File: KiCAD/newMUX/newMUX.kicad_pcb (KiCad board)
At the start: 4 copper layers, 17.8 x 30 mm, 13 parts, among them P1 CONN_02X07, P2 CONN_02X07, U1 MAX14662, U2 MAX14662, U3 PCF8574

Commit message: new mux done
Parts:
- removed G***: value, myParts:logo_small
- removed P1: CONN_02X07, myParts:SSM-107-L-DV
- removed P2: CONN_02X07, myParts:SSM-107-L-DV-INV
- removed R3, R4, R5, R6, R7: R, Resistors_SMD:R_0402
- added C1: 0.1uF, Capacitors_SMD:C_0603_HandSoldering, B.Cu at (47.0, -82.5)
- added J1: Conn_01x14, Pin_Headers:Pin_Header_Straight_1x14_Pitch2.54mm, B.Cu at (23.5, -61.0)
- added J2: Conn_02x06_Odd_Even, Socket_Strips:Socket_Strip_Straight_2x06_Pitch2.54mm, F.Cu at (35.9, -38.1)
- added J3: Conn_02x06_Odd_Even, Socket_Strips:Socket_Strip_Straight_2x06_Pitch2.54mm, F.Cu at (46.0, -38.1)
- added J4: Conn_01x14, Pin_Headers:Pin_Header_Straight_1x14_Pitch2.54mm, B.Cu at (61.0, -61.0)
- added JP1: Jumper_NC_Small, Connect:GS2, B.Cu at (27.9, -48.3)
- added JP2: Jumper_NC_Dual, Connect:GS3, B.Cu at (59.7, -85.1)
- added JP3: Jumper_NC_Dual, Connect:GS3, B.Cu at (57.1, -82.5)
- added JP4: Jumper_NC_Dual, Connect:GS3, B.Cu at (53.3, -85.1)
- added JP5: Jumper_NC_Dual, Connect:GS3, B.Cu at (52.1, -82.5)
- added JP6: Jumper_NC_Small, Connect:GS2, B.Cu at (57.1, -48.3)
- added L1: GREY@CHRISTOFORO.NET, myParts:logo, F.Cu at (27.3, -44.5)
- added U10: ASSR-1611, Housings_DIP:DIP-6_W7.62mm, F.Cu at (47.0, -24.1)
- added U11: ASSR-1611, Housings_DIP:DIP-6_W7.62mm, F.Cu at (31.8, -24.1)
- added U12: ASSR-1611, Housings_DIP:DIP-6_W7.62mm, F.Cu at (24.1, -68.6)
- added U13: ASSR-1611, Housings_DIP:DIP-6_W7.62mm, F.Cu at (31.8, -68.6)
- added U14: ASSR-1611, Housings_DIP:DIP-6_W7.62mm, F.Cu at (39.4, -68.6)
- added U15: ASSR-1611, Housings_DIP:DIP-6_W7.62mm, F.Cu at (47.0, -68.6)
- added U16: ASSR-1611, Housings_DIP:DIP-6_W7.62mm, F.Cu at (54.6, -68.6)
- added U17: ASSR-1611, Housings_DIP:DIP-6_W7.62mm, F.Cu at (31.8, -57.1)
- added U18: ASSR-1611, Housings_DIP:DIP-6_W7.62mm, F.Cu at (39.4, -57.1)
- added U19: ASSR-1611, Housings_DIP:DIP-6_W7.62mm, F.Cu at (47.0, -57.1)
- added U20: ASSR-1611, Housings_DIP:DIP-6_W7.62mm, F.Cu at (54.6, -12.7)
- added U21: ASSR-1611, Housings_DIP:DIP-6_W7.62mm, F.Cu at (24.1, -12.7)
- added U22: MCP23S17, Housings_DIP:DIP-28_W7.62mm, F.Cu at (25.4, -80.0)
- added U4: ASSR-1611, Housings_DIP:DIP-6_W7.62mm, F.Cu at (39.4, -1.27)
- added U5: ASSR-1611, Housings_DIP:DIP-6_W7.62mm, F.Cu at (47.0, -1.27)
- added U6: ASSR-1611, Housings_DIP:DIP-6_W7.62mm, F.Cu at (54.6, -1.27)
- added U7: ASSR-1611, Housings_DIP:DIP-6_W7.62mm, F.Cu at (31.8, -12.7)
- added U8: ASSR-1611, Housings_DIP:DIP-6_W7.62mm, F.Cu at (39.4, -12.7)
- added U9: ASSR-1611, Housings_DIP:DIP-6_W7.62mm, F.Cu at (47.0, -12.7)
- R1: value R -> 830K; footprint Resistors_SMD:R_0402 -> Resistors_SMD:R_2010_HandSoldering; moved to F.Cu
- R2: value R -> 500K; footprint Resistors_SMD:R_0402 -> Resistors_SMD:R_0805_HandSoldering
- U1, U2: value MAX14662 -> ASSR-1611; footprint Housings_DFN_QFN:QFN-28-1EP_4x4mm_Pitch0.4mm -> Housings_DIP:DIP-6_W7.62mm; moved to F.Cu
- U3: value PCF8574 -> ASSR-1611; footprint SMD_Packages:SO-16-W -> Housings_DIP:DIP-6_W7.62mm; moved to F.Cu
- moved R1 55.9 mm to (55.9, -28.6), turned to 90 degrees
- moved U1 47.8 mm to (39.4, -24.1), turned to 90 degrees
- moved R2 30.2 mm to (26.7, -24.2), turned to 90 degrees
- moved U3 21.2 mm to (31.8, -1.27), turned to 90 degrees
- moved U2 18.2 mm to (24.1, -1.27), turned to 90 degrees
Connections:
- R1 pad 1: +5V -> GND
- R1 pad 2: A0 -> /PRE_GND
- R2 pad 1: A0 -> Net-(R2-Pad1)
- R2 pad 2: GND -> V_D
- U1 pad 1: +5V -> /TOP
- U1 pad 2: L_I -> /PRE_GND
- U1 pad 3: 0_I -> (no net)
- U1 pad 4: 1_I -> V-
- U1 pad 5: 2_I -> (no net)
- U1 pad 6: 3_I -> /VT
- U2 pad 1: +5V -> /P1
- U2 pad 2: L_V -> /PRE_GND
- U2 pad 3: 0_V -> (no net)
- U2 pad 4: 1_V -> V+
- U2 pad 5: 2_V -> (no net)
- U2 pad 6: 3_V -> /V1
- U3 pad 1: A0 -> /P2
- U3 pad 2: A1 -> /PRE_GND
- U3 pad 3: A2 -> (no net)
- U3 pad 4: SM_CS -> V+
- U3 pad 5: Net-(U3-Pad5) -> (no net)
- U3 pad 6: Net-(U3-Pad6) -> /V2
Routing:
- net /PRE_GND: track 0.00 -> 196.8 mm, vias 0 -> 1
- net /BOT: track 0.00 -> 108.7 mm
- net /P3: track 0.00 -> 106.2 mm
- net /P5: track 0.00 -> 103.0 mm
- net /P4: track 0.00 -> 101.8 mm, vias 0 -> 3
- net V+: track 10.6 -> 105.6 mm
- net /P8: track 0.00 -> 87.8 mm, vias 0 -> 2
- net /TOP: track 0.00 -> 84.0 mm, vias 0 -> 3
- net /P2: track 0.00 -> 83.8 mm, vias 0 -> 1
- net /V_D_EN: track 0.00 -> 83.2 mm
- net /P7: track 0.00 -> 82.9 mm, vias 0 -> 1
- net /P1: track 0.00 -> 81.9 mm
- net V_D: track 0.00 -> 77.9 mm, vias 0 -> 2
- net /P6: track 0.00 -> 72.9 mm, vias 0 -> 2
- net MISO: track 0.00 -> 72.8 mm, vias 0 -> 2
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- added copper zone on B.Cu, net /PRE_GND
- added copper zone on F.Cu, net I+
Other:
- board size 17.8 x 30 mm -> 40 x 88.9 mm
- net class Default: clearance 0.153 -> 0.16; trace_width 0.25 -> 0.4; via_dia 0.8 -> 0.6
- rule trace_clearance: 0.153 -> 0.16
- rule trace_min: 0.18 -> 0.16
- board text removed: "17e0726"
- board text removed: "A0"
- board text removed: "A1"
- board text removed: "A2"
- board text removed: "H"
- board text removed: "L"

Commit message: generate order zip and silk for newMUX
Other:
- board text added: "ac10c1a"
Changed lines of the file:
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@@
-(kicad_pcb (version 4) (host pcbnew 4.0.6)
+(kicad_pcb (version 4) (host pcbnew 4.0.7)
   (general
     (links 127)
@@
     (area 22.149999 -88.975001 62.305001 0.075001)
     (thickness 1.6)
-    (drawings 8)
+    (drawings 9)
     (tracks 679)
     (zones 0)
@@
     (descr "6-lead dip package, row spacing 7.62 mm (300 mils)")
     (tags "DIL DIP PDIP 2.54mm 7.62mm 300mil")
-    (fp_text reference U17 (at 3.81 -2.39 90) (layer F.SilkS)
+    (fp_text reference U17 (at 3.81 0.635 90) (layer F.SilkS)
       (effects (font (size 1 1) (thickness 0.15)))
     )
@@
     (descr "6-lead dip package, row spacing 7.62 mm (300 mils)")
     (tags "DIL DIP PDIP 2.54mm 7.62mm 300mil")
-    (fp_text reference U18 (at 3.81 -2.39 90) (layer F.SilkS)
+    (fp_text reference U18 (at 3.81 0.635 90) (layer F.SilkS)
       (effects (font (size 1 1) (thickness 0.15)))
     )
@@
     (descr "6-lead dip package, row spacing 7.62 mm (300 mils)")
     (tags "DIL DIP PDIP 2.54mm 7.62mm 300mil")
-    (fp_text reference U19 (at 3.81 -2.39 90) (layer F.SilkS)
+    (fp_text reference U19 (at 3.81 0.635 90) (layer F.SilkS)
       (effects (font (size 1 1) (thickness 0.15)))
     )
@@
       (xy 8.293997 0.976563) (xy 8.491005 0.779554)) (layer F.SilkS) (width 0.001))
   )
+  (gr_text ac10c1a (at 30.48 -44.45 90) (layer F.SilkS)
+    (effects (font (size 1.5 1.5) (thickness 0.3)))
+  )
   (gr_arc (start 59.69 -2.54) (end 62.23 -2.54) (angle 90) (layer Edge.Cuts) (width 0.15))

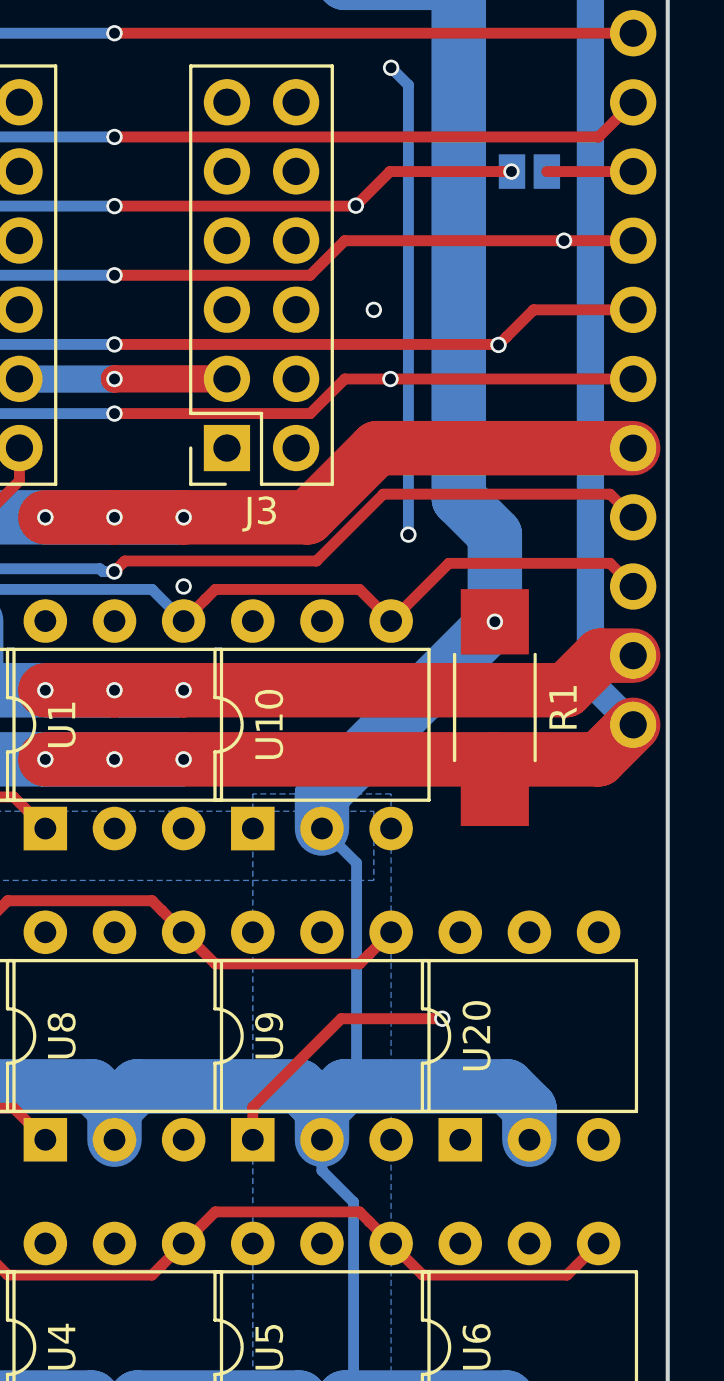
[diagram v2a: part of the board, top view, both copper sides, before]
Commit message: fixed some no-connect bugs in newMux
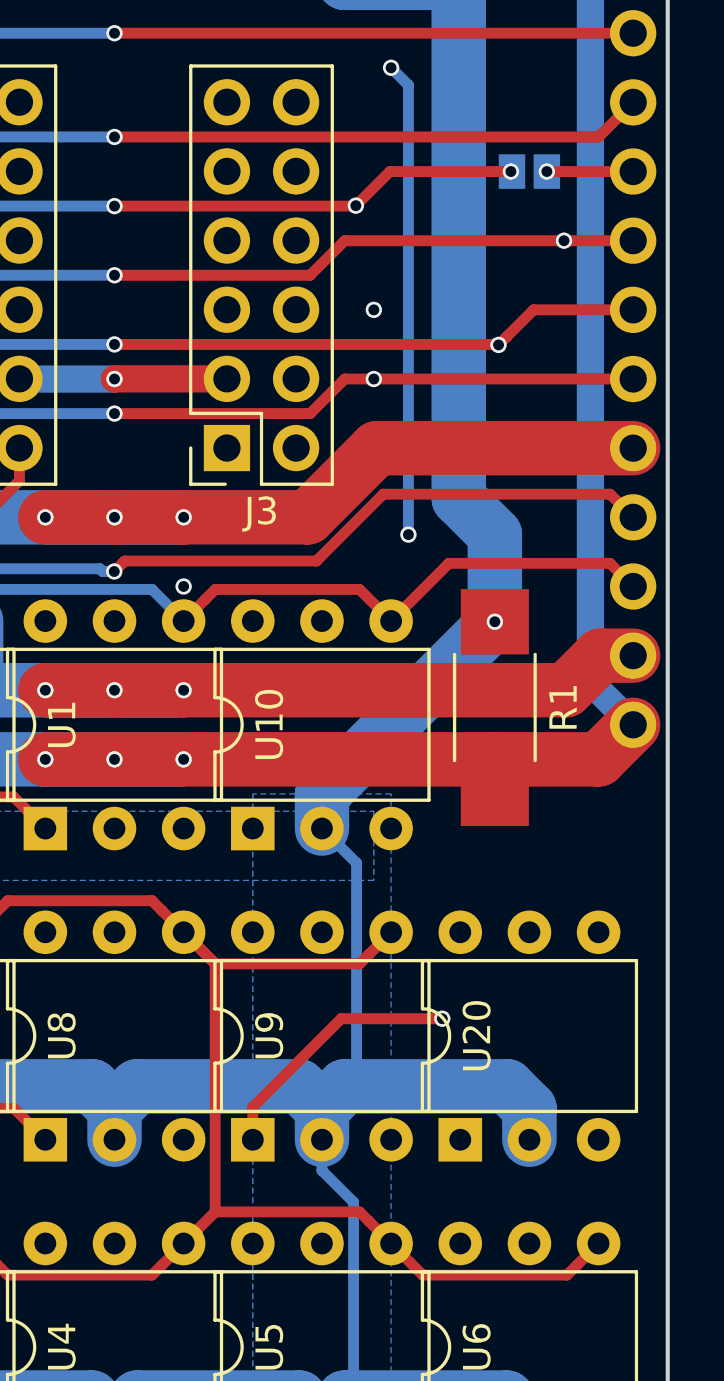
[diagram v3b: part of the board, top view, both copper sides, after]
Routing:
- net +5V: track 66.1 -> 107.5 mm
- net V+: track 105.6 -> 116.4 mm
- net SCK: track 78.4 -> 79.0 mm
- net Net-(J4-Pad6): track 3.18 -> 3.17 mm, vias 0 -> 1
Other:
- net class Default: trace_width 0.4 -> 0.25

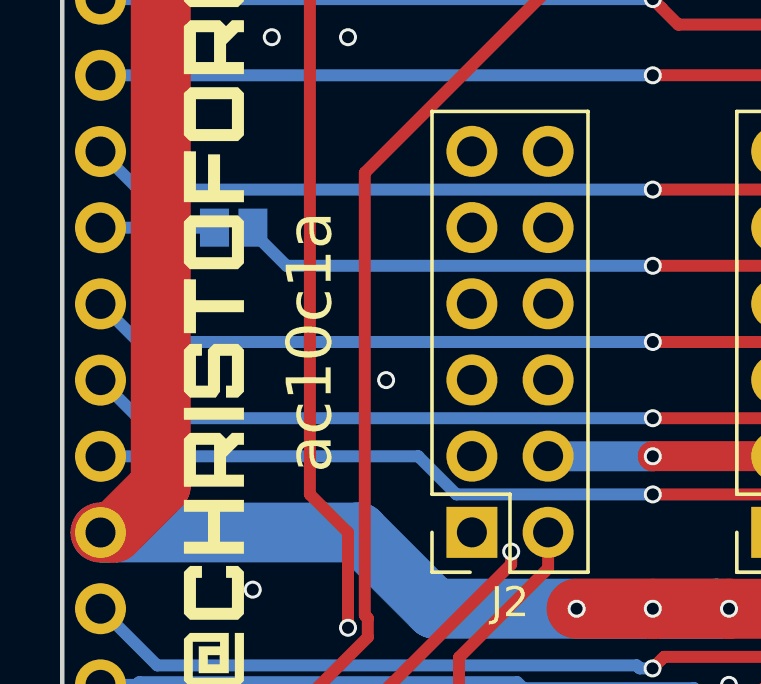
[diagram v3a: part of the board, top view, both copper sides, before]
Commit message: updated newMUX silk
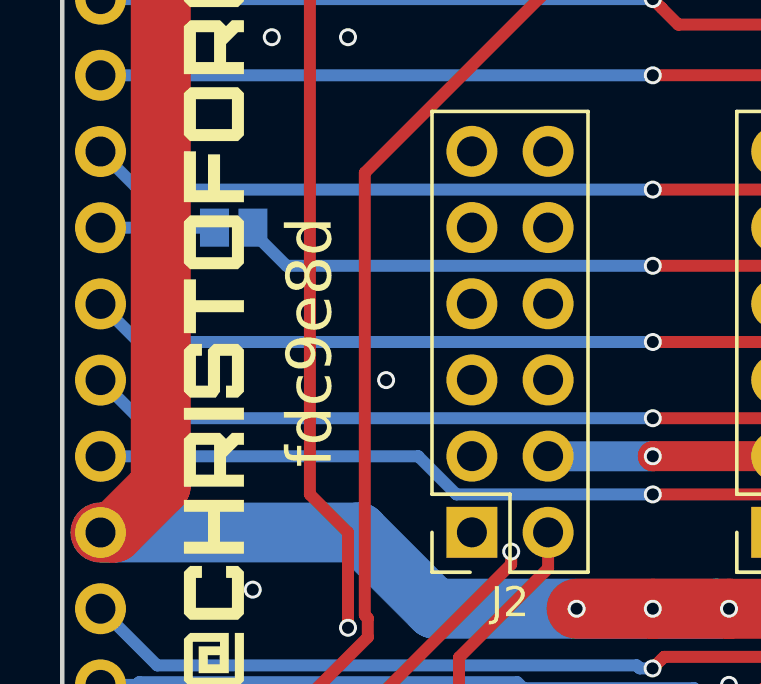
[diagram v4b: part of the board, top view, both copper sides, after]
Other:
- board text added: "fdc9e8d"
- board text removed: "ac10c1a"
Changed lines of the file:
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@@
       (xy 8.293997 0.976563) (xy 8.491005 0.779554)) (layer F.SilkS) (width 0.001))
   )
-  (gr_text ac10c1a (at 30.48 -44.45 90) (layer F.SilkS)
+  (gr_text fdc9e8d (at 30.48 -44.45 90) (layer F.SilkS)
     (effects (font (size 1.5 1.5) (thickness 0.3)))
   )

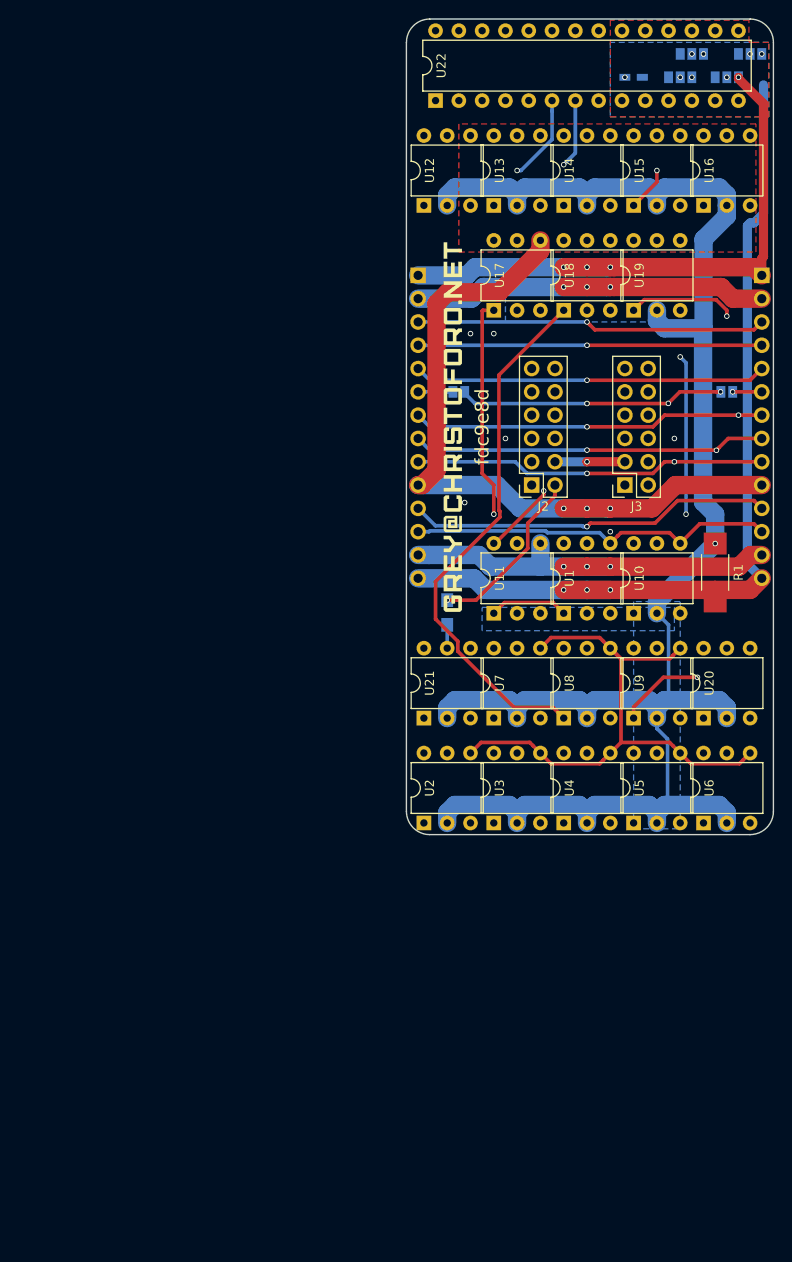
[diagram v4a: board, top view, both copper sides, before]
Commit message: fixed up newMux so that parts don't collide
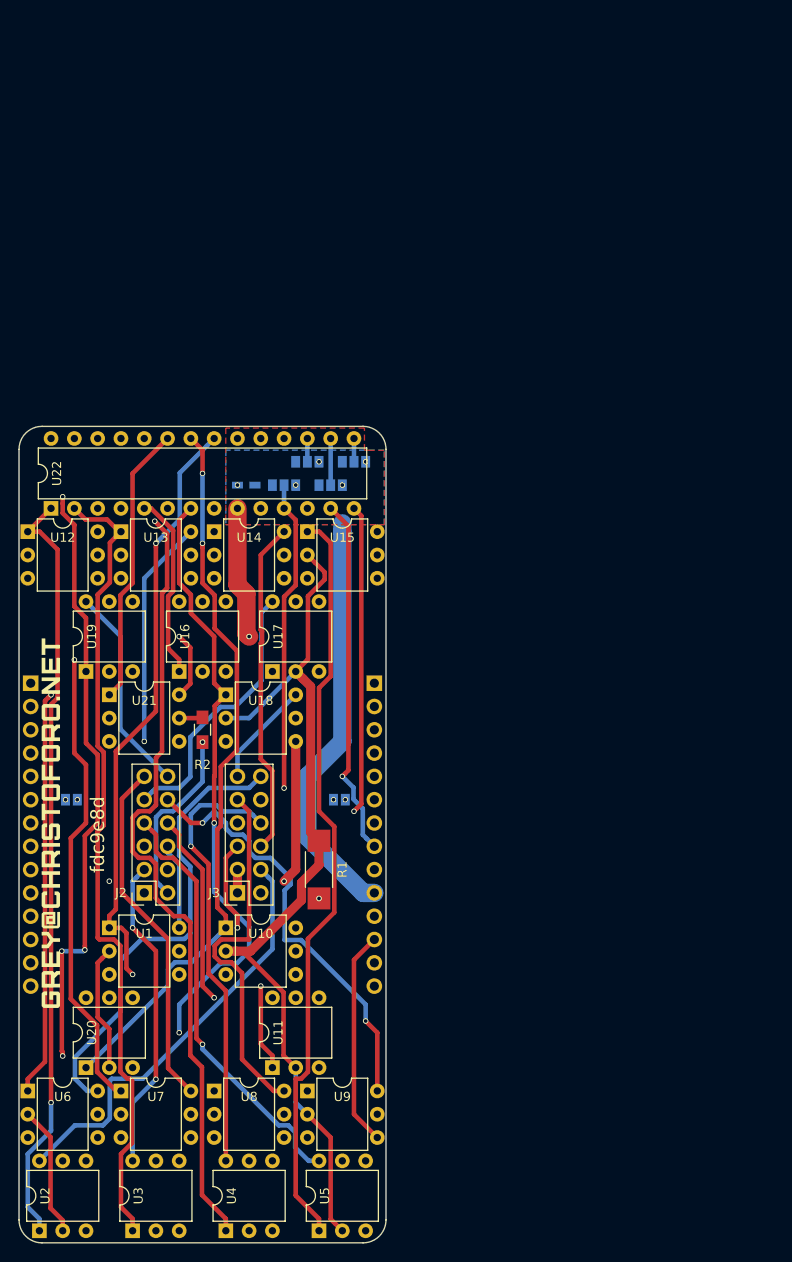
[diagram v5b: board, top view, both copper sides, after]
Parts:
- R2: moved to F.Cu
- moved U6 79.2 mm to (-19.1, 27.9), turned to 0 degrees
- moved U20 77.3 mm to (-12.7, 25.4)
- moved U16 76.5 mm to (-2.54, -17.8)
- moved U19 71.5 mm to (-12.7, -17.8)
- moved JP3 62.0 mm to (14.0, -38.1)
- moved JP5 62.0 mm to (8.89, -38.1)
- moved JP2 62.0 mm to (16.5, -40.6)
- moved L1 61.5 mm to (-16.5, -1.27)
- moved C1 61.3 mm to (4.76, -38.1)
- moved J1 61.3 mm to (-18.7, -16.5)
- moved J2 61.3 mm to (-6.35, 6.35)
- moved J3 61.3 mm to (3.81, 6.35)
- moved J4 61.3 mm to (18.7, -16.5)
- moved JP1 61.3 mm to (-14.3, -3.81)
- moved JP6 61.3 mm to (14.9, -3.81)
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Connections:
- J1 pad 10: I+ -> GND
- J1 pad 11: V+ -> I+
- J1 pad 12: V- -> V+
- J1 pad 13: I- -> V-
- J1 pad 14: GND -> I-
- J4 pad 10: I+ -> GND
- J4 pad 11: V+ -> I+
- J4 pad 12: V- -> V+
- J4 pad 13: I- -> V-
- J4 pad 14: GND -> I-
- U1 pad 3: (no net) -> Net-(U1-Pad3)
- U1 pad 5: (no net) -> Net-(U1-Pad5)
- U10 pad 3: (no net) -> Net-(U10-Pad3)
- U10 pad 5: (no net) -> Net-(U10-Pad5)
- U11 pad 3: (no net) -> Net-(U11-Pad3)
- U11 pad 5: (no net) -> Net-(U11-Pad5)
- U12 pad 3: (no net) -> Net-(U12-Pad3)
- U12 pad 5: (no net) -> Net-(U12-Pad5)
- U13 pad 3: (no net) -> Net-(U13-Pad3)
- U13 pad 5: (no net) -> Net-(U13-Pad5)
- U14 pad 3: (no net) -> Net-(U14-Pad3)
- U14 pad 5: (no net) -> Net-(U14-Pad5)
- U15 pad 3: (no net) -> Net-(U15-Pad3)
- U15 pad 5: (no net) -> Net-(U15-Pad5)
- U16 pad 3: (no net) -> Net-(U16-Pad3)
- U16 pad 5: (no net) -> Net-(U16-Pad5)
- U17 pad 3: (no net) -> Net-(U17-Pad3)
- U17 pad 5: (no net) -> Net-(U17-Pad5)
- U18 pad 3: (no net) -> Net-(U18-Pad3)
- U18 pad 5: (no net) -> Net-(U18-Pad5)
- U19 pad 3: (no net) -> Net-(U19-Pad3)
- U19 pad 5: (no net) -> Net-(U19-Pad5)
- U2 pad 3: (no net) -> Net-(U2-Pad3)
- U2 pad 5: (no net) -> Net-(U2-Pad5)
- U20 pad 3: (no net) -> Net-(U20-Pad3)
- U20 pad 5: (no net) -> Net-(U20-Pad5)
- U21 pad 3: (no net) -> Net-(U21-Pad3)
- U21 pad 4: (no net) -> Net-(U21-Pad4)
- U22 pad 19: (no net) -> Net-(U22-Pad19)
- U22 pad 20: (no net) -> Net-(U22-Pad20)
- U22 pad 24: (no net) -> Net-(U22-Pad24)
- U22 pad 25: (no net) -> Net-(U22-Pad25)
- U22 pad 26: (no net) -> Net-(U22-Pad26)
- U22 pad 27: (no net) -> Net-(U22-Pad27)
- U22 pad 28: (no net) -> Net-(U22-Pad28)
- U3 pad 3: (no net) -> Net-(U3-Pad3)
- U3 pad 5: (no net) -> Net-(U3-Pad5)
- U4 pad 3: (no net) -> Net-(U4-Pad3)
- U4 pad 5: (no net) -> Net-(U4-Pad5)
- U5 pad 3: (no net) -> Net-(U5-Pad3)
- U5 pad 5: (no net) -> Net-(U5-Pad5)
- U6 pad 3: (no net) -> Net-(U6-Pad3)
- U6 pad 5: (no net) -> Net-(U6-Pad5)
- U7 pad 3: (no net) -> Net-(U7-Pad3)
- U7 pad 5: (no net) -> Net-(U7-Pad5)
- U8 pad 3: (no net) -> Net-(U8-Pad3)
- U8 pad 5: (no net) -> Net-(U8-Pad5)
- U9 pad 3: (no net) -> Net-(U9-Pad3)
- U9 pad 5: (no net) -> Net-(U9-Pad5)
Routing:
- net /PRE_GND: track 196.8 -> 281.3 mm, vias 1 -> 0
- net I+: track 80.4 -> 133.2 mm, vias 3 -> 1
- net /V_D_EN: track 83.2 -> 30.6 mm
- net +5V: track 107.5 -> 66.9 mm, vias 8 -> 7
- net GND: track 132.5 -> 96.9 mm, vias 4 -> 1
- net /BOT: track 108.7 -> 79.3 mm, vias 0 -> 2
- net /P8: track 87.8 -> 113.8 mm, vias 2 -> 4
- net /I4: track 40.1 -> 64.1 mm
- net /V2: track 56.1 -> 34.4 mm, vias 0 -> 2
- net /P5: track 103.0 -> 81.4 mm, vias 0 -> 1
- net /P6: track 72.9 -> 94.1 mm, vias 2 -> 1
- net /V1: track 66.1 -> 46.6 mm
- net V_D: track 77.9 -> 58.6 mm, vias 2 -> 1
- net /V8: track 33.2 -> 47.8 mm, vias 0 -> 2
- net V+: track 116.4 -> 103.1 mm, vias 1 -> 0
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- removed copper zone on B.Cu, net /PRE_GND
- removed copper zone on F.Cu, net I+
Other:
- board size 40 x 88.9 mm -> 40 x 89 mm
- net class Default: trace_width 0.25 -> 0.5

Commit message: update silk
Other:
- net class Default: trace_width 0.5 -> 0.25
- board text added: "1ad7c5f"
- board text removed: "fdc9e8d"
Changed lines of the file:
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@@
   )
   (setup
-    (last_trace_width 0.5)
+    (last_trace_width 0.25)
     (user_trace_width 1)
     (user_trace_width 2)
@@
   (net_class Default "This is the default net class."
     (clearance 0.16)
-    (trace_width 0.5)
+    (trace_width 0.25)
     (via_dia 0.6)
     (via_drill 0.4)
@@
   (gr_arc (start -17.5 -42) (end -17.5 -44.5) (angle -90) (layer Edge.Cuts) (width 0.15))
   (gr_arc (start 17.5 -42) (end 20 -42) (angle -90) (layer Edge.Cuts) (width 0.15))
-  (gr_text fdc9e8d (at -11.43 0 90) (layer F.SilkS)
+  (gr_text 1ad7c5f (at -11.43 0 90) (layer F.SilkS)
     (effects (font (size 1.5 1.5) (thickness 0.3)))
   )
